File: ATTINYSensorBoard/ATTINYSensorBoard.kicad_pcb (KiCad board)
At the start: 2 copper layers, 17 parts, among them J1 ICSP, J2 POWER/CAN, U1 ATtiny841-SS, U2 MCP25625-x-SS, U3 74HC04

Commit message: Started PCB layout
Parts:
- moved U2 43.2 mm to (179.9, 102.5)
- moved J2 39.9 mm to (166.4, 81.9)
- moved U1 33.0 mm to (161.9, 99.0), turned to 90 degrees
- moved JP1 30.7 mm to (151.8, 106.0), turned to -90 degrees
- moved U3 26.3 mm to (162.0, 108.2), turned to 90 degrees
- moved JP2 24.7 mm to (151.8, 102.2), turned to -90 degrees
- moved JP3 18.7 mm to (151.8, 98.4), turned to -90 degrees
- moved J1 4.02 mm to (142.2, 99.7)

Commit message: Finished Sensor Board Template
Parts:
- added J3: Conn_01x04, Connector_PinHeader_2.54mm:PinHeader_1x04_P2.54mm_Vertical, F.Cu at (127.0, 97.8)
- C6, C7, U1, U3: moved to B.Cu
- moved C1 41.4 mm to (153.5, 102.0), turned to 90 degrees
- moved U2 37.0 mm to (143.0, 104.8), turned to 180 degrees
- moved C4 36.1 mm to (145.5, 111.5), turned to 180 degrees
- moved C3 35.7 mm to (140.6, 111.5)
- moved C7 33.8 mm to (151.9, 109.2), turned to 180 degrees
- moved C2 28.5 mm to (137.2, 102.2), turned to -90 degrees
- moved U1 22.3 mm to (140.4, 104.8), turned to 180 degrees
- moved J2 21.5 mm to (156.4, 101.0)
- moved C6 21.5 mm to (141.7, 99.1)
- moved JP3 21.2 mm to (131.6, 104.8), turned to 90 degrees
- moved D1 20.9 mm to (152.7, 107.3), turned to 180 degrees
- moved JP1 20.3 mm to (131.6, 108.6), turned to 90 degrees
- moved JP2 20.2 mm to (131.6, 101.0), turned to 90 degrees
- moved C5 16.5 mm to (137.3, 93.7), turned to -90 degrees
- moved R1 16.2 mm to (149.4, 107.3), turned to -90 degrees
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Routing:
- net +5V: track 0.00 -> 100.3 mm, vias 0 -> 1
- net /MISO: track 0.00 -> 33.7 mm
- net GND: track 0.00 -> 33.2 mm, vias 0 -> 8
- net /MOSI: track 0.00 -> 32.9 mm, vias 0 -> 1
- net Net-(JP1-B): track 0.00 -> 24.5 mm, vias 0 -> 1
- net /SCK: track 0.00 -> 21.8 mm
- net /USER0: track 0.00 -> 13.5 mm
- net /~{RESET}: track 0.00 -> 13.4 mm
- net /USER3: track 0.00 -> 12.8 mm
- net /USER1: track 0.00 -> 12.2 mm
- net /USER2: track 0.00 -> 11.7 mm
- net /CAN_P: track 0.00 -> 11.2 mm
- net /CAN_N: track 0.00 -> 11.2 mm
- net /~{SS}: track 0.00 -> 10.3 mm, vias 0 -> 1
- net /STBY: track 0.00 -> 9.74 mm, vias 0 -> 1
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- added copper zone on B.Cu, net GND
- added copper zone on F.Cu, net GND
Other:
- board outline added: 50.8 x 25.4 mm
- board text added: "5V GND CANH CANL"
- board text added: "CANBUS Sensor Input Module"
- board text added: "DISCONNECT FOR ICSP"
- board text added: "ICSP"
- board text added: "JP1, JP2, JP3"
- board text added: "PA0/10"
- board text added: "PA1/9"
- board text added: "PA2/8"
- board text added: "PA3/7"
- board text added: "POWER CANBUS"
- board text added: "SENSOR CONNECTOR TO INPUT PINS"
- board text added: "TEMPLATE"
- board text added: "© 2024 NCSU Baja"

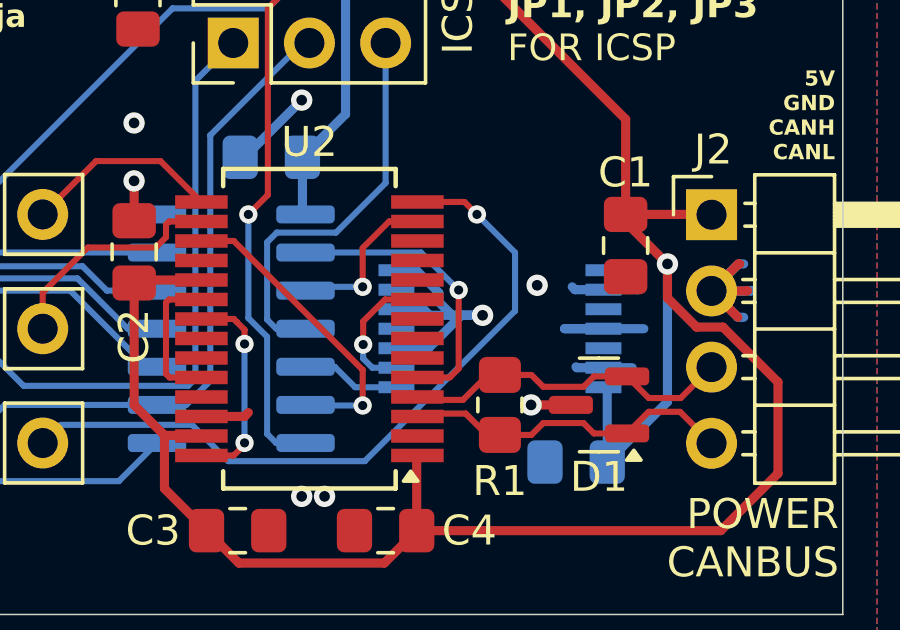
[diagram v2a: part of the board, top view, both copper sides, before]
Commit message: Fixed grounds
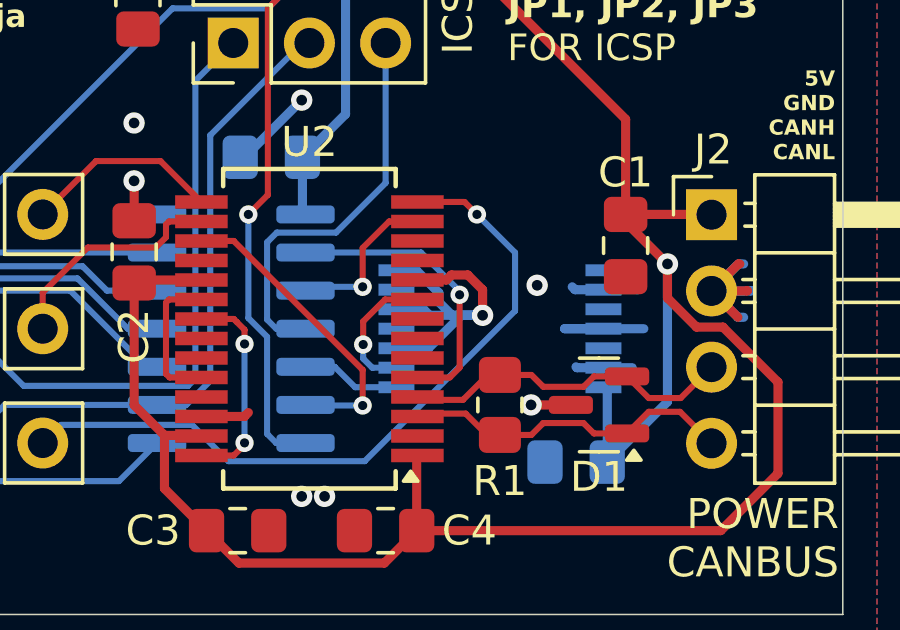
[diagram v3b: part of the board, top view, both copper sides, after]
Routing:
- net GND: track 33.2 -> 36.5 mm
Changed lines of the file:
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@@
+	)
+	(segment
+		(start 147.738141 102.98334)
+		(end 148.285235 102.98334)
+		(width 0.3048)
+		(layer "F.Cu")
+		(net 1)
 	)
 	(segment
@@
 	)
 	(segment
+		(start 146.605 103.15)
+		(end 147.571481 103.15)
+		(width 0.3048)
+		(layer "F.Cu")
+		(net 1)
+	)
+	(segment
+		(start 147.571481 103.15)
+		(end 147.738141 102.98334)
+		(width 0.3048)
+		(layer "F.Cu")
+		(net 1)
+	)
+	(segment
+		(start 148.285235 102.98334)
+		(end 148.777826 103.475931)
+		(width 0.3048)
+		(layer "F.Cu")
+		(net 1)
+	)
+	(segment
 		(start 156.41 103.515)
 		(end 157.597 103.515)
@@
 		(start 139.405 107.7)
 		(end 140.839 107.7)
+		(width 0.3048)
+		(layer "F.Cu")
+		(net 1)
+	)
+	(segment
+		(start 148.777826 103.475931)
+		(end 148.777826 104.327826)
 		(width 0.3048)
 		(layer "F.Cu")
@@
 	)
 	(segment
-		(start 147.979911 103.484701)
-		(end 147.979911 106.103289)
+		(start 148.011688 106.071512)
+		(end 147.6832 106.4)
+		(width 0.2032)
+		(layer "F.Cu")
+		(net 12)
+	)
+	(segment
+		(start 148.011688 103.64374)
+		(end 148.011688 106.071512)
 		(width 0.2032)
 		(layer "F.Cu")
@@
 		(net 12)
 	)
-	(segment
-		(start 147.979911 106.103289)
-		(end 147.6832 106.4)
-		(width 0.2032)
-		(layer "F.Cu")
-		(net 12)
-	)
 	(via
-		(at 147.979911 103.484701)
+		(at 148.011688 103.64374)
 		(size 0.6096)
 		(drill 0.3048)
@@
 	)
 	(segment
-		(start 147.979911 103.484701)
-		(end 147.974301 103.484701)
-		(width 0.2032)
-		(layer "B.Cu")
-		(net 12)
-	)
-	(segment
 		(start 146.7246 102.235)
 		(end 142.875 102.235)
@@
 	)
 	(segment
-		(start 147.974301 103.484701)
+		(start 148.011688 103.64374)
+		(end 148.011688 103.522088)
+		(width 0.2032)
+		(layer "B.Cu")
+		(net 12)
+	)
+	(segment
+		(start 148.011688 103.522088)
 		(end 146.7246 102.235)
 		(width 0.2032)
